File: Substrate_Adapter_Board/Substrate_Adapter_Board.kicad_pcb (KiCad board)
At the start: 2 copper layers, 7.8 x 5.3 mm, 3 parts, among them J1 Conn_02x04_Top_Bottom, U1 W25Q128JVS, U2 W25Q128JVS

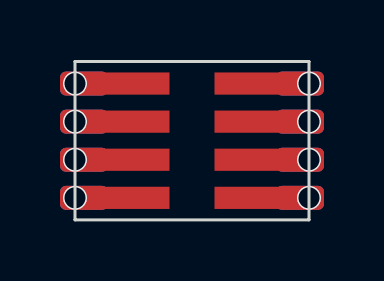
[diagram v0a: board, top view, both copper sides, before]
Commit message: adjust pcb width to 7.9mm
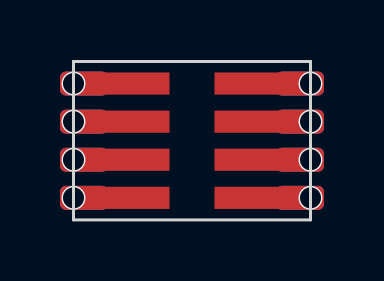
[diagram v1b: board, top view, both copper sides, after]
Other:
- board size 7.8 x 5.3 mm -> 7.9 x 5.3 mm
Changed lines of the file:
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@@
       (net 8 "VCC") (pinfunction "~{CS}") (pintype "input"))
   )
-  (gr_rect (start 139.53 76.01) (end 147.33 81.29) (layer "Edge.Cuts") (width 0.1) (fill none))
-  (dimension (type aligned) (layer "Dwgs.User")
-    (pts (xy 139.53 81.29) (xy 147.33 81.29))
-    (height 2.495)
-    (gr_text "7.8000 mm" (at 143.43 82.685) (layer "Dwgs.User")
-      (effects (font (size 1 1) (thickness 0.1)))
-    )
-    (format (units 3) (units_format 1) (precision 4))
-    (style (thickness 0.1) (arrow_length 1.27) (text_position_mode 0) (extension_height 0.58642) (extension_offset 0.5) keep_text_aligned)
-  )
+  (gr_rect (start 139.48 76.01) (end 147.38 81.29) (layer "Edge.Cuts") (width 0.1) (fill none))
   (dimension (type aligned) (layer "Dwgs.User")
     (pts (xy 147.33 76.01) (xy 147.33 81.29))
@@
     (style (thickness 0.1) (arrow_length 1.27) (text_position_mode 0) (extension_height 0.58642) (extension_offset 0.5) keep_text_aligned)
   )
-  (via (at 139.53 76.745) (size 0.8) (drill 0.7) (layers "F.Cu" "B.Cu") (net 1))
-  (via (at 139.53 78.015) (size 0.8) (drill 0.7) (layers "F.Cu" "B.Cu") (net 2))
-  (via (at 139.53 79.285) (size 0.8) (drill 0.7) (layers "F.Cu" "B.Cu") (net 3))
-  (via (at 139.53 80.555) (size 0.8) (drill 0.7) (layers "F.Cu" "B.Cu") (net 4))
-  (via (at 147.33 80.555) (size 0.8) (drill 0.7) (layers "F.Cu" "B.Cu") (net 5))
-  (via (at 147.33 79.285) (size 0.8) (drill 0.7) (layers "F.Cu" "B.Cu") (net 6))
-  (via (at 147.33 78.015) (size 0.8) (drill 0.7) (layers "F.Cu" "B.Cu") (net 7))
-  (via (at 147.33 76.745) (size 0.8) (drill 0.7) (layers "F.Cu" "B.Cu") (net 8))
+  (dimension (type aligned) (layer "Dwgs.User")
+    (pts (xy 139.48 81.29) (xy 147.38 81.29))
+    (height 2.84)
+    (gr_text "7.9000 mm" (at 143.43 83.03) (layer "Dwgs.User")
+      (effects (font (size 1 1) (thickness 0.1)))
+    )
+    (format (units 3) (units_format 1) (precision 4))
+    (style (thickness 0.1) (arrow_length 1.27) (text_position_mode 0) (extension_height 0.58642) (extension_offset 0.5) keep_text_aligned)
+  )
+  (via (at 139.48 76.745) (size 0.8) (drill 0.7) (layers "F.Cu" "B.Cu") (net 1))
+  (via (at 139.48 78.015) (size 0.8) (drill 0.7) (layers "F.Cu" "B.Cu") (net 2))
+  (via (at 139.48 79.285) (size 0.8) (drill 0.7) (layers "F.Cu" "B.Cu") (net 3))
+  (via (at 139.48 80.555) (size 0.8) (drill 0.7) (layers "F.Cu" "B.Cu") (net 4))
+  (via (at 147.38 80.555) (size 0.8) (drill 0.7) (layers "F.Cu" "B.Cu") (net 5))
+  (via (at 147.38 79.285) (size 0.8) (drill 0.7) (layers "F.Cu" "B.Cu") (net 6))
+  (via (at 147.38 78.015) (size 0.8) (drill 0.7) (layers "F.Cu" "B.Cu") (net 7))
+  (via (at 147.38 76.745) (size 0.8) (drill 0.7) (layers "F.Cu" "B.Cu") (net 8))
 )
